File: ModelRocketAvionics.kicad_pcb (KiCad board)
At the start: 4 copper layers, 60 x 60 mm, 60 parts, among them P1 USB_C_Plug, Q2 AO3400A, Q3 AO3400A, SW2 SW_SPDT, U1 ICM-42605, U2 W25Q16JVSS, U3 BMP280, U5 STM32F411, U6 L86-M33, U7 915MHz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

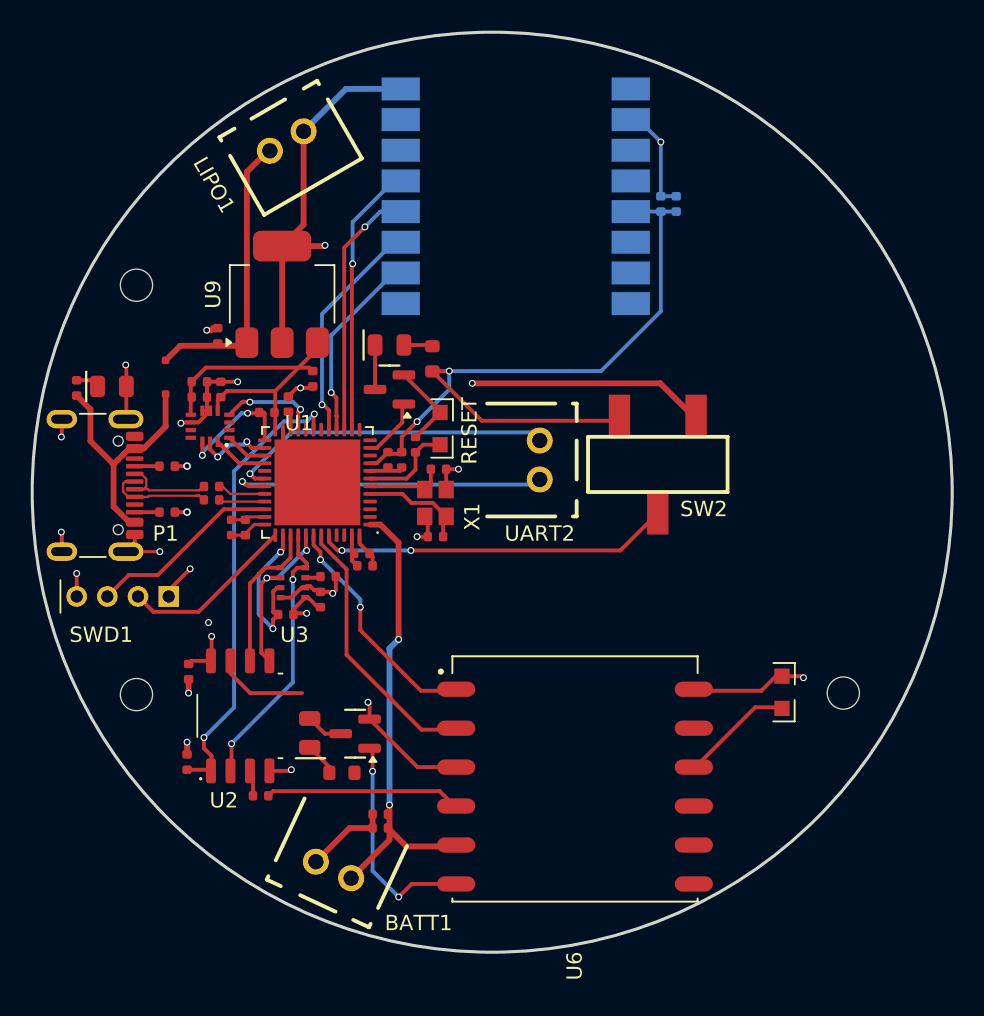
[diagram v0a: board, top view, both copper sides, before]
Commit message: Added more room for antenna pin on LoRa
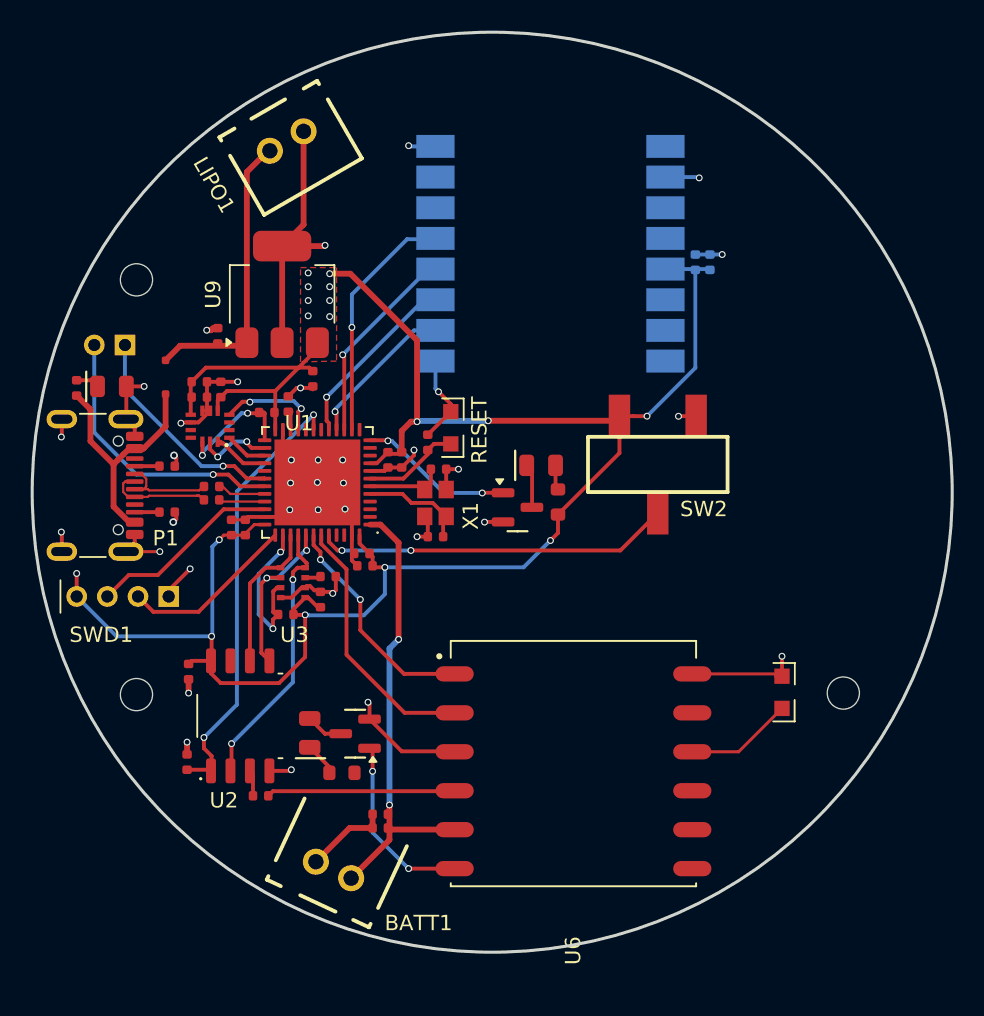
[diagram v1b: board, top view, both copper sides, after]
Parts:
- removed UART2: Connector, easyeda2kicad:CONN-TH_B2B-XH-A-LF-SN
- added REF**: PinHeader_2x01_P2.00mm_Vertical, Connector_PinHeader_2.00mm:PinHeader_2x01_P2.00mm_Vertical, F.Cu at (140.1, 34.9)
- moved D5 12.6 mm to (167.2, 42.8)
- moved R5 12.4 mm to (168.3, 45.1)
- moved Q2 11.3 mm to (165.7, 45.5), turned to 0 degrees
- moved C28 4.42 mm to (177.2, 29.5)
- moved C3 4.39 mm to (178.2, 29.5)
- moved U7 4.38 mm to (167.8, 28.9)
- moved U6 1.00 mm to (169.3, 62.7)
- moved C27 0.81 mm to (159.8, 41.2)
- moved REF** 0.70 mm to (161.3, 39.2)
- moved REF** 0.70 mm to (161.3, 41.4)
- moved REF** 0.35 mm to (140.8, 30.6)
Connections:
- U5 pad 11: Net-(Q2-G) -> unconnected-(U5-PA1-Pad11)
- U5 pad 12: /MCU_TX2 -> Net-(Q2-G)
- U5 pad 13: /MCU_RX2 -> unconnected-(U5-PA3-Pad13)
- U7 pad 9: Net-(AE1-A) -> unconnected-(U7-ANT-Pad9)
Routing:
- net +3.3V: track 98.3 -> 153.5 mm, vias 6 -> 18
- net GND: track 119.8 -> 108.9 mm, vias 21 -> 35
- net /Debug_TX: track 21.5 -> 14.4 mm
- net Net-(Q2-G): track 4.03 -> 10.1 mm, vias 0 -> 2
- net Net-(U2-~{HOLD}/~{RESET}/IO_{3}): track 6.02 -> 0.00 mm
- net /SPI1_SCK: track 16.5 -> 13.3 mm
- net /SPI1_MOSI: track 14.9 -> 11.9 mm
- net /Debug_RX: track 21.2 -> 18.3 mm, vias 2 -> 1
- net Net-(Q3-G): track 14.6 -> 11.9 mm
- net /SPI1_MISO: track 12.5 -> 10.0 mm
- net /SPI1_NSS: track 17.8 -> 15.8 mm
- net /MCU_RX1: track 17.7 -> 16.1 mm
- net /SPI5_NSS: track 30.0 -> 29.0 mm
- net +BATT: track 30.5 -> 29.9 mm
- added copper zone on F.Cu, net +3.3V

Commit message: Added RP2040 compatible branch, addded battery protection circuitry
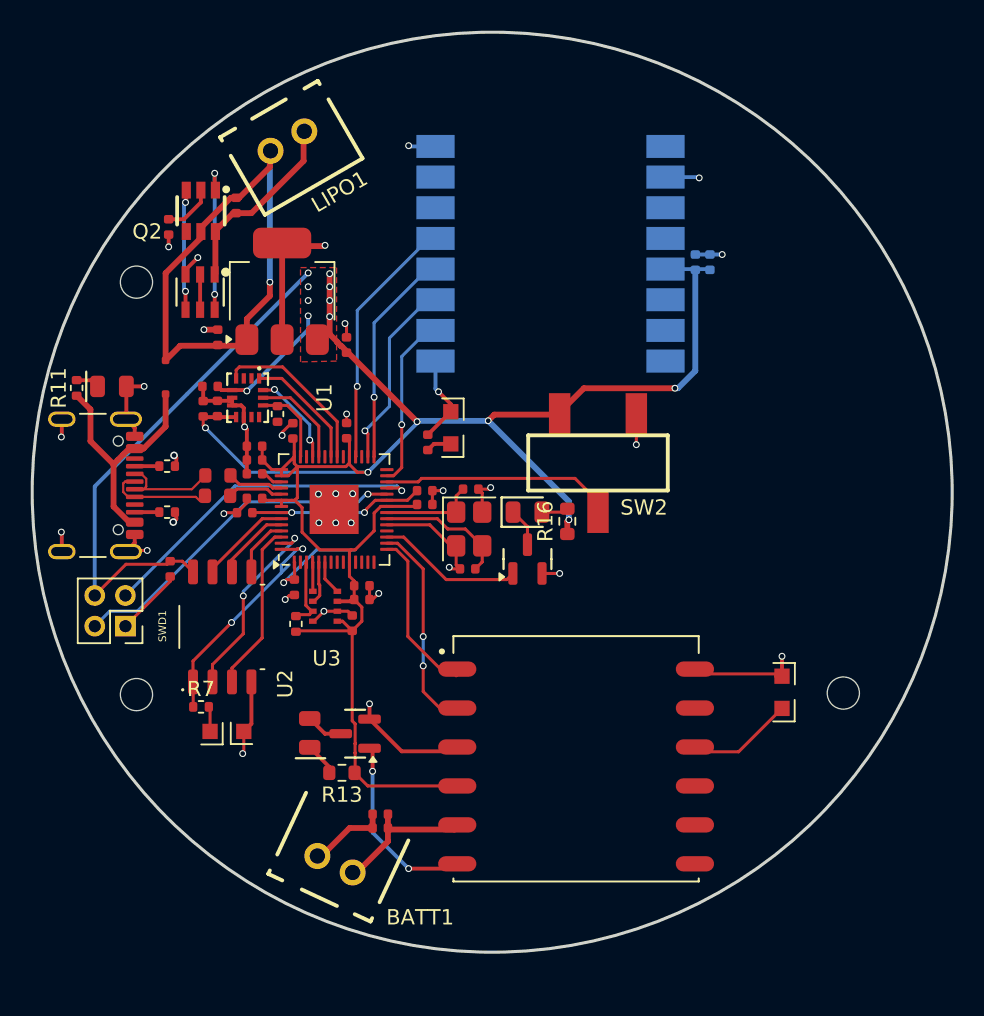
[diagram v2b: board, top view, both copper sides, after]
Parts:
- removed C21: 1uF, PCM_JLCPCB:C_0402
- removed C26: 4.7uF, PCM_JLCPCB:C_0402
- removed D5: Red, PCM_JLCPCB:D_0805
- removed R14, R6: 22Ω, PCM_JLCPCB:R_0402
- removed R5: 75Ω, PCM_JLCPCB:R_0603
- removed R9: 5.1kΩ, PCM_JLCPCB:R_0402
- removed the REF** at (140.1, 34.9)
- removed U5: STM32F411, Package_DFN_QFN:QFN-48-1EP_7x7mm_P0.5mm_EP5.6x5.6mm
- added C13: 100nF, PCM_JLCPCB:C_0402, F.Cu at (159.6, 45.3)
- added C14: 100nF, PCM_JLCPCB:C_0402, F.Cu at (148.5, 42.4)
- added C16: 100nF, PCM_JLCPCB:C_0402, F.Cu at (154.5, 40.5)
- added C19: 100nF, PCM_JLCPCB:C_0402, F.Cu at (159.6, 44.4)
- added C2: 100nF, PCM_JLCPCB:C_0402, F.Cu at (151.1, 50.7)
- added C22: 1uF, PCM_JLCPCB:C_0402, F.Cu at (147.9, 45.8)
- added C23: 1uF, PCM_JLCPCB:C_0402, F.Cu at (148.5, 44.9)
- added D2: Red, PCM_JLCPCB:D_0805, F.Cu at (166.3, 45.8)
- added Q1: AO3400A, PCM_JLCPCB:Q_SOT-23, F.Cu at (166.3, 48.9)
- added R10: 5.1kΩ, Resistor_SMD:R_0402_1005Metric, F.Cu at (151.2, 53.1)
- added R16: 75Ω, Resistor_SMD:R_0603_1608Metric, F.Cu at (168.9, 46.4)
- added R17: 27Ω, PCM_JLCPCB:R_0603, F.Cu at (146.1, 44.7)
- added R18: 27Ω, PCM_JLCPCB:R_0603, F.Cu at (146.1, 43.4)
- added R4: 2kΩ, PCM_JLCPCB:R_0402, F.Cu at (142.9, 27.2)
- added REF**: TestPoint_Pad_1.0x1.0mm, TestPoint:TestPoint_Pad_1.0x1.0mm, F.Cu at (147.8, 60.1)
- added REF**: TestPoint_Pad_1.0x1.0mm, TestPoint:TestPoint_Pad_1.0x1.0mm, F.Cu at (145.6, 60.1)
- added U4: RP2040, Package_DFN_QFN:QFN-56-1EP_7x7mm_P0.4mm_EP3.2x3.2mm, F.Cu at (153.7, 45.6)
- C10, C11: value 20pF -> 15pF
- C18: value 4.7uF -> 100nF
- P1: footprint USB-C:USB-C -> Connector_USB:USB_C_Receptacle_GCT_USB4105-xx-A_16P_TopMnt_Horizontal
- Q2: value AO3400A -> NCE8205; footprint PCM_JLCPCB:Q_SOT-23 -> easyeda2kicad:SOT-23-6_L2.9-W1.6-P0.95-LS2.8-BL
- R1, R11, R12, R2, R7: footprint PCM_JLCPCB:R_0402 -> Resistor_SMD:R_0402_1005Metric
- R13: footprint PCM_JLCPCB:R_0603 -> Resistor_SMD:R_0603_1608Metric
- R3: value 5.1kΩ -> FM2113_C2832124; footprint PCM_JLCPCB:R_0402 -> easyeda2kicad:SOT-23-6_L2.9-W1.6-P0.95-LS2.8-BR
- SWD1: footprint Connector_PinHeader_2.00mm:PinHeader_1x04_P2.00mm_Vertical -> Connector_PinHeader_2.00mm:PinHeader_2x02_P2.00mm_Vertical
- X1: value Shenzhen SCTF Elec SX2B12.000F1010F30 -> Crystal_GND24_Small; footprint Crystal:Crystal_SMD_2520-4Pin_2.5x2.0mm -> Crystal:Crystal_SMD_3225-4Pin_3.2x2.5mm
- moved R3 38.3 mm to (145.0, 26.1), turned to 90 degrees
- moved Q2 25.0 mm to (144.9, 31.4), turned to 180 degrees
- moved C20 19.3 mm to (147.3, 25.8), turned to 90 degrees
- moved C25 10.6 mm to (148.5, 41.5), turned to 180 degrees
- moved C9 9.31 mm to (155.5, 50.6), turned to 0 degrees
- moved C18 8.72 mm to (148.5, 43.3)
- moved C29 7.02 mm to (151.0, 40.5), turned to 90 degrees
- moved C1 6.81 mm to (143.0, 49.5)
- moved C11 6.77 mm to (162.4, 49.5), turned to 0 degrees
- moved U2 5.92 mm to (146.4, 53.3)
- moved SW2 3.90 mm to (170.9, 42.6)
- moved C10 3.86 mm to (162.6, 44.3)
- moved R7 3.71 mm to (145.0, 58.5), turned to 0 degrees
- moved SWD1 3.42 mm to (140.1, 53.2), turned to 180 degrees
- moved C4 3.11 mm to (154.5, 34.9), turned to 90 degrees
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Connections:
- net /SPI2_NSS renamed /SPI1_CSn
- net /SPI5_NSS renamed /QSPI_NSS
- C10 pad 1: Net-(U5-PH0-OSC_IN) -> GND
- C10 pad 2: GND -> /XOUT
- C11 pad 2: Net-(U5-PH1-OSC_OUT) -> /XIN
- C18 pad 1: +3.3V -> +1V1
- C20 pad 1: +3.3V -> -1S LiPo
- C20 pad 2: GND -> +1S LiPo
- C25 pad 1: GND -> +3.3V
- C25 pad 2: +3.3V -> GND
- C27 pad 1: Net-(U5-NRST) -> Net-(C27-Pad1)
- C29 pad 1: GND -> +3.3V
- C29 pad 2: +3.3V -> GND
- C5 pad 1: +3.7V -> +1S LiPo
- C9 pad 1: GND -> +3.3V
- C9 pad 2: +3.3V -> GND
- D1 pad 1: +3.7V -> +1S LiPo
- LIPO1 pad 1: +3.7V -> +1S LiPo
- LIPO1 pad 2: GND -> -1S LiPo
- Q2 pad 1: Net-(Q2-G) -> -1S LiPo
- Q2 pad 2: GND -> Net-(Q2-D-Pad2)
- Q2 pad 3: Net-(Q2-D) -> GND
- R3 pad 1: Net-(U2-~{WP}/IO_{2}) -> Net-(Q2-G1)
- R3 pad 2: +3.3V -> Net-(R3-CS)
- R7 pad 2: +3.3V -> Net-(JP1-B)
- U1 pad 1: /SPI2_MISO -> /SPI1_RX
- U1 pad 13: /SPI2_SCK -> /SPI1_SCK
- U1 pad 14: /SPI2_MOSI -> /SPI1_TX
- U2 pad 2: /SPI3_MISO -> /QSPI_SD1
- U2 pad 3: Net-(U2-~{WP}/IO_{2}) -> /QSPI_SD2
- U2 pad 5: /SPI3_MOSI -> /QSPI_SD0
- U2 pad 6: /SPI3_SCK -> /QSPI_SCLK
- U2 pad 7: Net-(U2-~{HOLD}/~{RESET}/IO_{3}) -> /QSPI_SD3
- U3 pad 2: /SPI3_NSS -> /SPI0_CSn
- U3 pad 3: /SPI3_MOSI -> /SPI0_TX
- U3 pad 4: /SPI3_SCK -> /SPI0_SCK
- U3 pad 5: /SPI3_MISO -> /SPI0_RX
- U6 pad 1: /MCU_TX1 -> /UART0_TX
- U6 pad 2: /MCU_RX1 -> /UART0_RX
- U7 pad 2: /SPI1_MISO -> /SPI0_RX
- U7 pad 3: /SPI1_MOSI -> /SPI0_TX
- U7 pad 4: /SPI1_SCK -> /SPI0_SCK
- U7 pad 5: /SPI1_NSS -> /SPI0_CSn
- U9 pad 1: +3.7V -> +1S LiPo
- X1 pad 1: Net-(U5-PH1-OSC_OUT) -> /XOUT
- X1 pad 3: Net-(U5-PH0-OSC_IN) -> /XIN
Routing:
- net +1S LiPo: track 0.00 -> 35.5 mm, vias 0 -> 1
- net +3.3V: track 153.5 -> 180.1 mm, vias 18 -> 16
- net /SPI0_CSn: track 0.00 -> 21.2 mm, vias 0 -> 1
- net +BATT: track 29.9 -> 9.93 mm, vias 2 -> 0
- net +3.7V: track 19.0 -> 0.00 mm
- net /Debug_RX: track 18.3 -> 0.00 mm, vias 1 -> 0
- net /SPI3_MISO: track 18.0 -> 0.00 mm, vias 2 -> 0
- net /MCU_RX1: track 16.1 -> 0.00 mm
- net /SPI0_SCK: track 0.00 -> 16.1 mm, vias 0 -> 1
- net /SPI1_NSS: track 15.8 -> 0.00 mm, vias 1 -> 0
- net /SPI0_TX: track 0.00 -> 15.3 mm, vias 0 -> 1
- net /MCU_TX1: track 14.9 -> 0.00 mm, vias 2 -> 0
- net /Debug_TX: track 14.4 -> 0.00 mm, vias 1 -> 0
- net /UART0_RX: track 0.00 -> 14.0 mm, vias 0 -> 2
- net /SPI0_RX: track 0.00 -> 13.6 mm, vias 0 -> 1
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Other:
- board text removed: "RESET"

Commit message: Overhauled layout, added more clearance for antenna.
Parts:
- removed C27: 100nF, PCM_JLCPCB:C_0402
- removed the REF** at (161.3, 39.2)
- removed the REF** at (161.3, 41.4)
- added R9: 5.1kΩ, Resistor_SMD:R_0402_1005Metric, F.Cu at (154.8, 52.8)
- C28, C3, U7: moved to F.Cu
- moved Q2 23.7 mm to (164.4, 17.9), turned to 90 degrees
- moved R4 22.9 mm to (162.9, 15.9), turned to 0 degrees
- moved SWD1 22.9 mm to (159.5, 41.0), turned to 90 degrees
- moved R3 17.6 mm to (160.6, 17.9), turned to 0 degrees
- moved R10 17.4 mm to (157.5, 36.9), turned to 180 degrees
- moved C20 12.9 mm to (157.8, 18.4)
- moved R16 3.94 mm to (165.9, 43.9), turned to 180 degrees
- moved U3 3.65 mm to (156.8, 51.8)
- moved C17 2.69 mm to (156.8, 53.9), turned to 180 degrees
- moved C12 2.58 mm to (156.8, 54.8), turned to 180 degrees
- moved C4 2.38 mm to (152.7, 36.5), turned to 180 degrees
- moved SW1 1.87 mm to (172.7, 43.1), turned to -90 degrees
- moved C9 1.78 mm to (153.8, 50.2), turned to 180 degrees
- moved R13 1.75 mm to (154.3, 61.0)
- moved D6 1.75 mm to (152.1, 58.5)
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- renumbered SW2 to SW1
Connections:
- R12 pad 2: /SPI1_CSn -> /SPI0_CSn
- SWD1 pad 1: GND -> /SWDIO
- SWD1 pad 2: /SWCLK -> GND
- SWD1 pad 3: /SWDIO -> /SWCLK
- U1 pad 1: /SPI1_RX -> /SPI0_RX
- U1 pad 12: /SPI1_CSn -> /SPI0_CSn
- U1 pad 13: /SPI1_SCK -> /SPI0_SCK
- U1 pad 14: /SPI1_TX -> /SPI0_TX
- U3 pad 2: /SPI0_CSn -> /SPI1_CSn
- U3 pad 3: /SPI0_TX -> /SPI1_TX
- U3 pad 4: /SPI0_SCK -> /SPI1_SCK
- U3 pad 5: /SPI0_RX -> /SPI1_RX
- U4 pad 35: /SPI0_TX -> /IMU_INT
- U4 pad 41: /SPI1_CSn -> /IMU_INT
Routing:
- net /SPI0_RX: track 13.6 -> 32.4 mm, vias 1 -> 2
- net /SWDIO: track 22.1 -> 4.42 mm, vias 1 -> 0
- net /SWCLK: track 22.6 -> 5.85 mm, vias 1 -> 0
- net /SPI0_TX: track 15.3 -> 30.2 mm, vias 1 -> 2
- net /IMU_INT: track 0.00 -> 13.2 mm, vias 0 -> 2
- net GND: track 98.7 -> 86.3 mm, vias 36 -> 42
- net /SPI0_SCK: track 16.1 -> 27.2 mm, vias 1 -> 2
- net (no net): track 11.0 -> 0.00 mm
- net Net-(Q2-G1): track 10.0 -> 1.35 mm, vias 2 -> 0
- net /USB_FS_DN: track 6.70 -> 0.00 mm
- net Net-(Q2-G2): track 7.90 -> 1.35 mm, vias 2 -> 0
- net Net-(SW1-B): track 15.6 -> 21.9 mm, vias 0 -> 2
- net +1S LiPo: track 35.5 -> 30.9 mm, vias 1 -> 0
- net /SPI1_SCK: track 6.40 -> 1.88 mm
- net /USB_FS_DP: track 6.63 -> 2.24 mm
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- added copper zone on F.Cu, net GND
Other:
- board text added: "PROTECTION"
- board text added: "RESET"

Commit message: Fixed layout of Schematic and pin labelling.
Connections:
- net /XIN renamed Net-(U4-XIN)
- net /XOUT renamed Net-(U4-XOUT)
- R10 pad 2: /SPI0_CSn -> /SPI0_CS1
- R12 pad 2: /SPI0_CSn -> /SPI0_CS2
- U1 pad 12: /SPI0_CSn -> /SPI0_CS2
- U4 pad 18: /SPI1_TX -> unconnected-(U4-GPIO15-Pad18)
- U4 pad 2: /SPI0_RX -> unconnected-(U4-GPIO0-Pad2)
- U4 pad 27: /SPI0_RX -> unconnected-(U4-GPIO16-Pad27)
- U4 pad 28: /SPI0_CSn -> /SPI0_CS1
- U4 pad 3: /SPI0_CSn -> unconnected-(U4-GPIO1-Pad3)
- U4 pad 32: /SPI0_CSn -> /SPI0_CS2
- U4 pad 34: /SPI0_SCK -> unconnected-(U4-GPIO22-Pad34)
- U4 pad 35: /IMU_INT -> unconnected-(U4-GPIO23-Pad35)
- U4 pad 36: /SPI1_RX -> unconnected-(U4-GPIO24-Pad36)
- U4 pad 37: /SPI1_CSn -> unconnected-(U4-GPIO25-Pad37)
- U4 pad 38: /SPI1_SCK -> unconnected-(U4-GPIO26_ADC0-Pad38)
- U4 pad 39: /SPI1_TX -> unconnected-(U4-GPIO27_ADC1-Pad39)
- U4 pad 4: /SPI0_SCK -> unconnected-(U4-GPIO2-Pad4)
- U4 pad 40: /SPI1_RX -> unconnected-(U4-GPIO28_ADC2-Pad40)
- U4 pad 43: +3.3V -> Net-(U4-ADC_AVDD)
- U4 pad 44: +3.3V -> Net-(U4-ADC_AVDD)
- U4 pad 48: +3.3V -> Net-(U4-ADC_AVDD)
- U4 pad 5: /SPI0_TX -> unconnected-(U4-GPIO3-Pad5)
- U4 pad 6: /SPI0_RX -> unconnected-(U4-GPIO4-Pad6)
- U4 pad 7: /SPI0_CSn -> unconnected-(U4-GPIO5-Pad7)
- U4 pad 8: /SPI0_SCK -> unconnected-(U4-GPIO6-Pad8)
- U4 pad 9: /SPI0_TX -> unconnected-(U4-GPIO7-Pad9)
- U7 pad 5: /SPI0_CSn -> /SPI0_CS1
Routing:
- net /SPI0_CSn: track 23.4 -> 0.00 mm
- net /SPI0_CS1: track 0.00 -> 15.1 mm
- net /SPI0_CS2: track 0.00 -> 8.28 mm
